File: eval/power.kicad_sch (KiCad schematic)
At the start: 20 parts, among them Q1 BSC0702LS, Q2 BSC0702LS, U2 LM5148RGYR

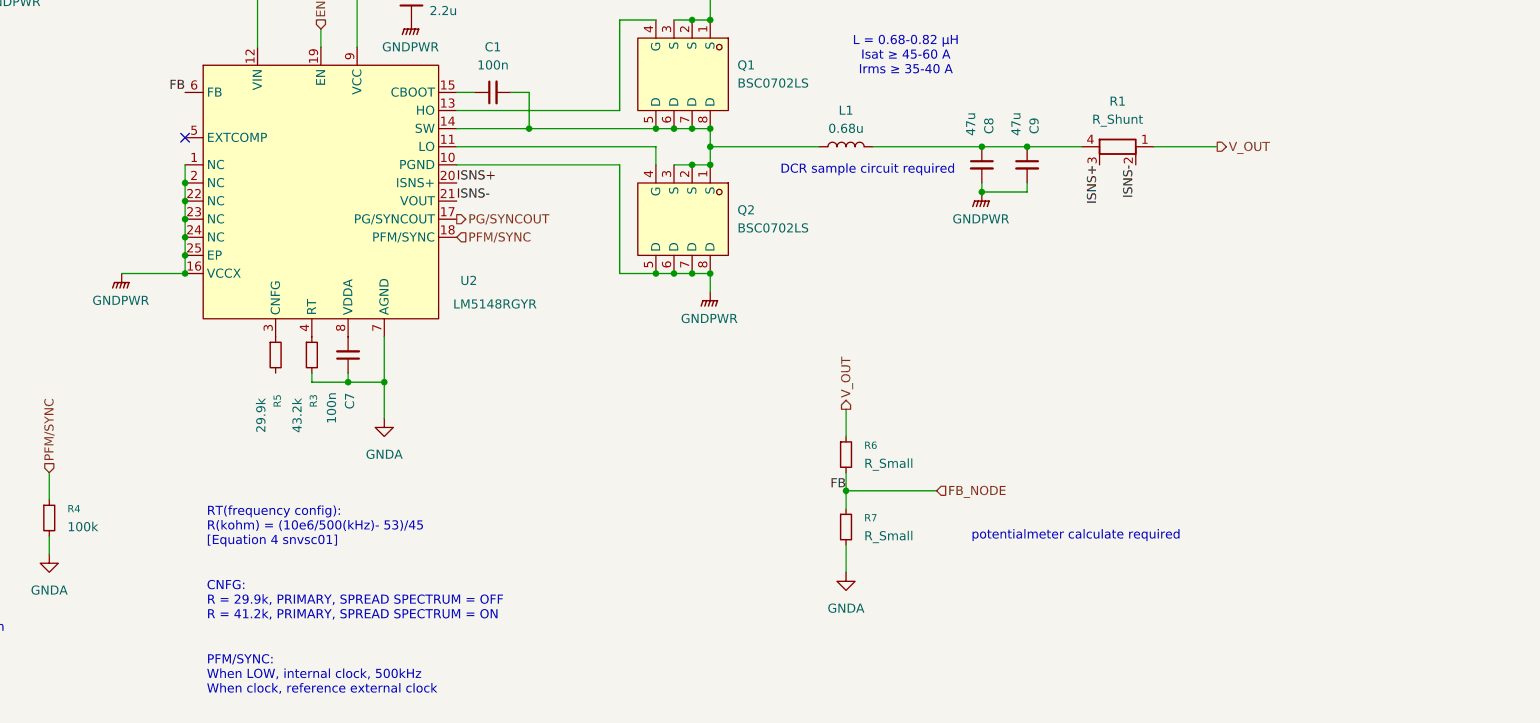
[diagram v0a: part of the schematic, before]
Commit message: Update constant current loop in kicad, base on simluation
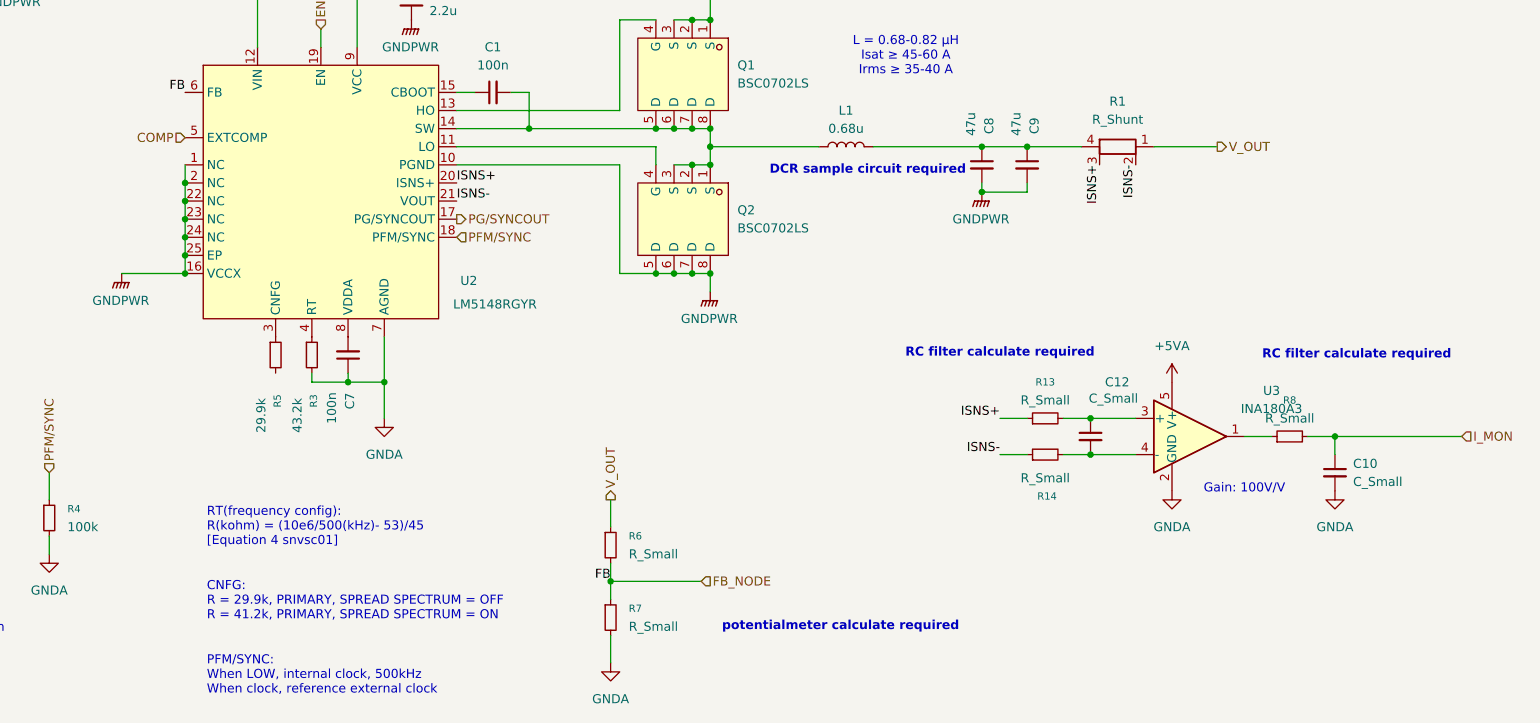
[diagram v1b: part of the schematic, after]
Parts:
- added C10, C12: C_Small, symbol Device:C_Small
- added R13, R14, R8: R_Small, symbol Device:R_Small
- added U3: INA180A3, Package_TO_SOT_SMD:SOT-23-5, symbol Amplifier_Current:INA180A3
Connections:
- net GNDA: now also C10.2, U3.2 (GND)
- net ISNS+: now also R13.1
- net ISNS-: now also R14.1
- net COMP: now reaches U2.5 (EXTCOMP)
- new net: C12.2, R14.2, U3.4 (-)
- new net: C12.1, R13.2, U3.3 (+)
- new net: R8.1, U3.1
- new net +5VA: U3.5 (V+)
- new net I_MON: C10.1, R8.2
- no-connect marks 1 -> 0
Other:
- note added: "Gain: 100V/V"
- note added: "RC filter calculate required"
- moved on the sheet: R6, R7

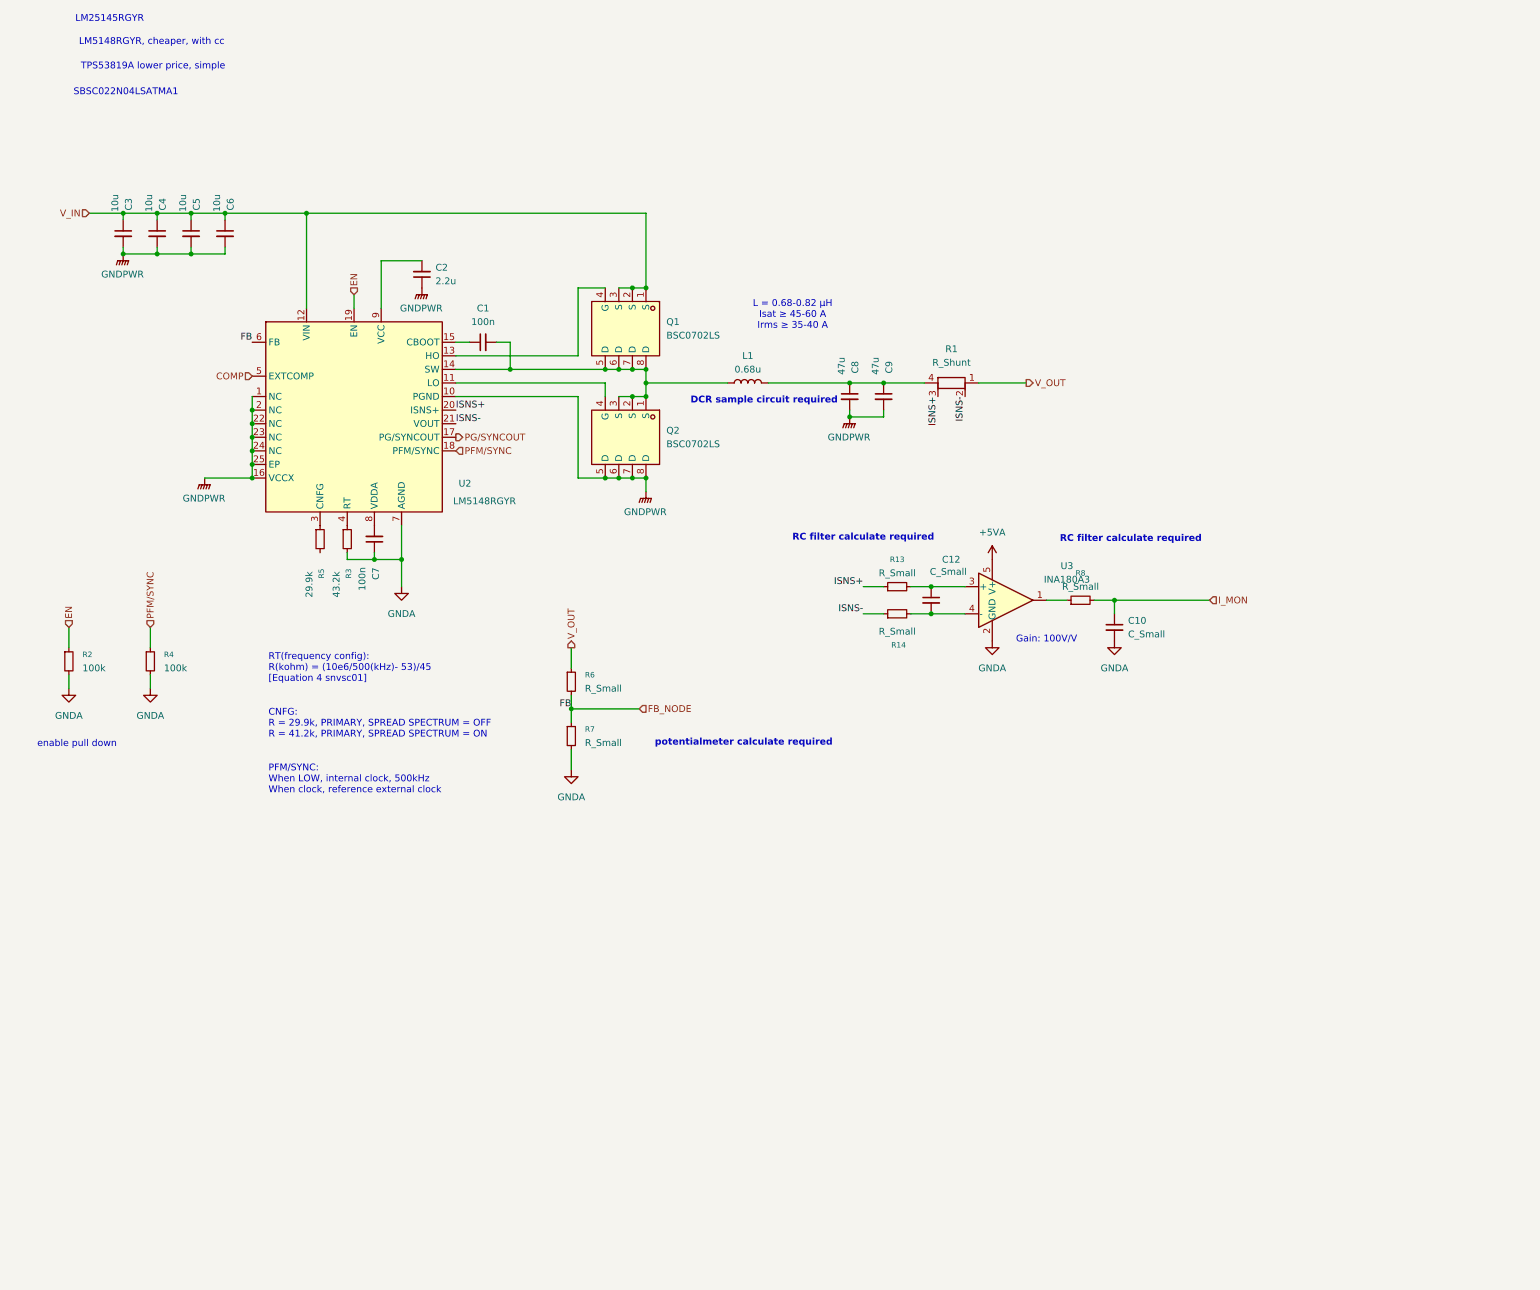
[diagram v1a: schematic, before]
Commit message: Change from G071 to G0B1, add screen, usb
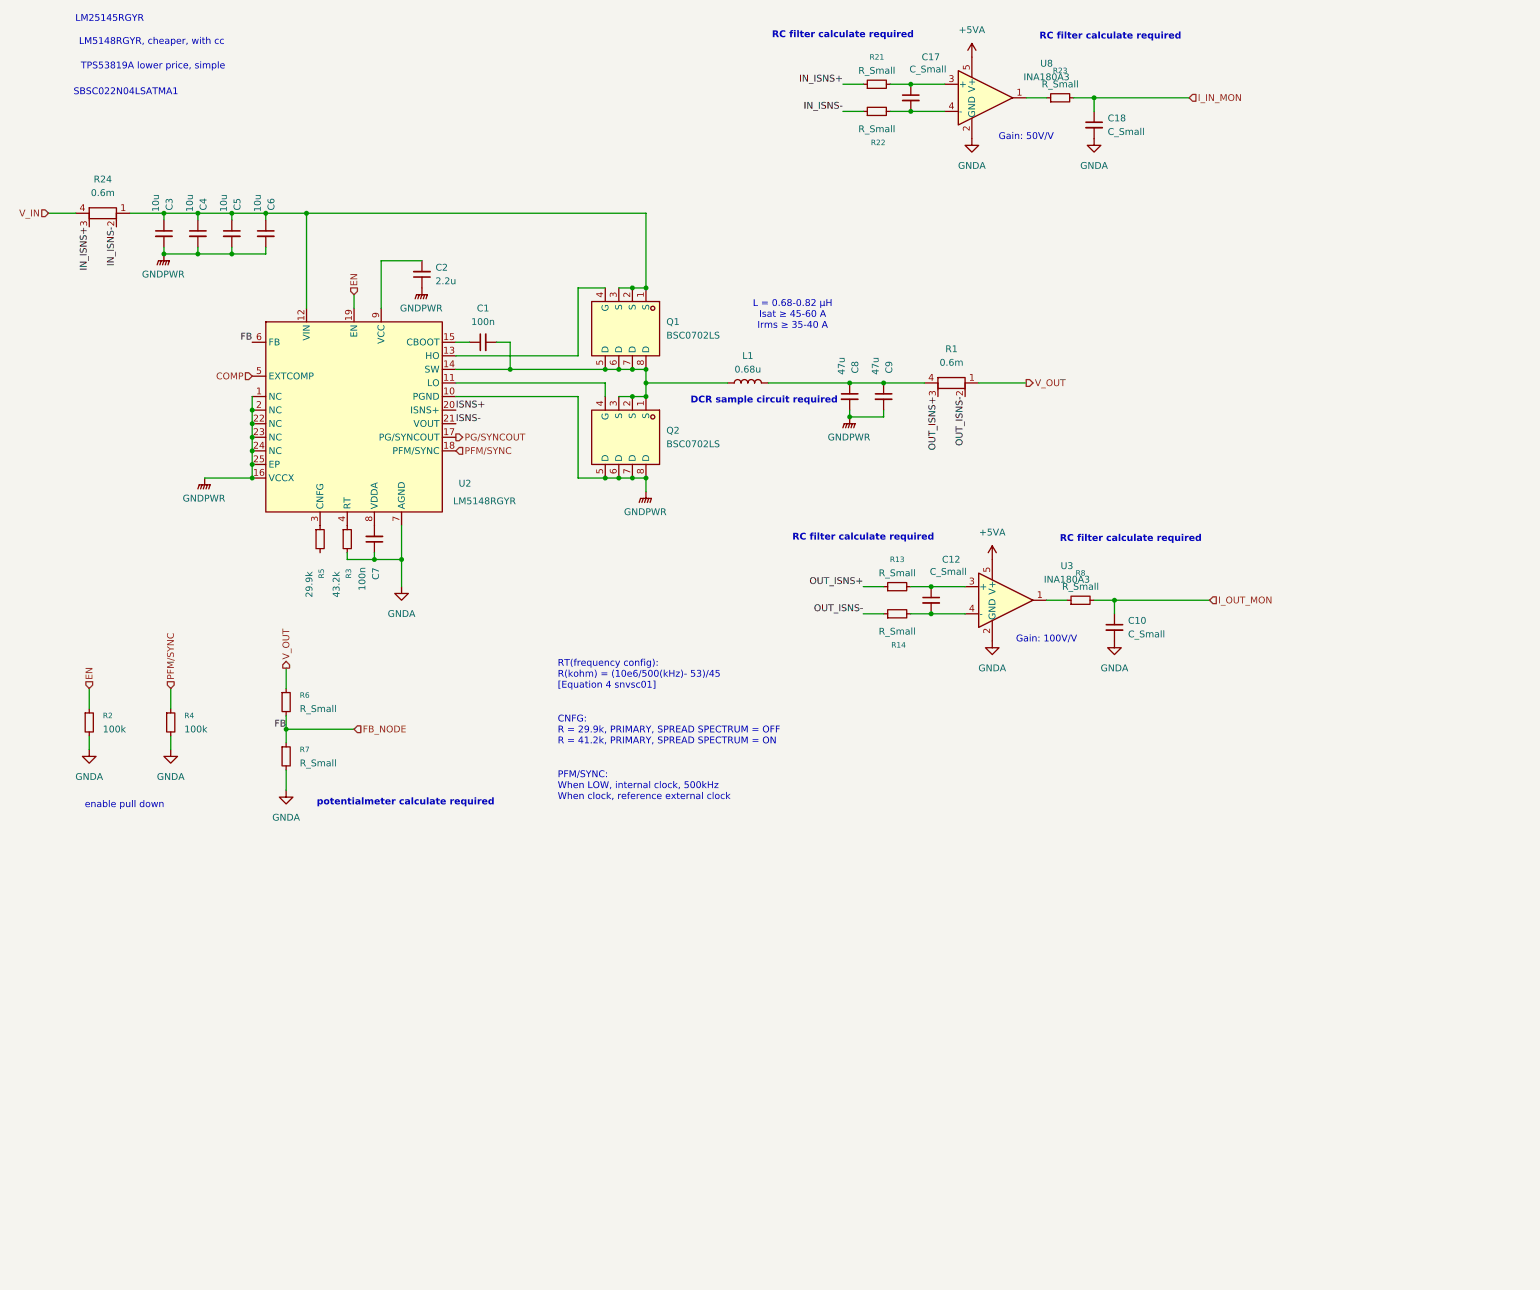
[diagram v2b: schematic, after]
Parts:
- added C17, C18: C_Small, symbol Device:C_Small
- added R21, R22, R23: R_Small, symbol Device:R_Small
- added R24: 0.6m, symbol Device:R_Shunt
- added U8: INA180A3, Package_TO_SOT_SMD:SOT-23-5, symbol Amplifier_Current:INA180A3
- R1: value R_Shunt -> 0.6m
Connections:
- net +5VA: now also U8.5 (V+)
- net GNDA: now also C18.2, U8.2 (GND)
- net ISNS+: no longer R1.3, R13.1
- net ISNS-: no longer R1.2, R14.1
- net V_IN: now also R24.4; no longer C3.1, C4.1, C5.1, C6.1, Q1.1 (S), Q1.2 (S), Q1.3 (S), U2.12 (VIN)
- net I_MON renamed I_OUT_MON
- new net: C17.1, R21.2, U8.3 (+)
- new net: C3.1, C4.1, C5.1, C6.1, Q1.1 (S), Q1.2 (S), Q1.3 (S), R24.1, U2.12 (VIN)
- new net: R23.1, U8.1
- new net: C17.2, R22.2, U8.4 (-)
- new net IN_ISNS+: R21.1, R24.3
- new net IN_ISNS-: R22.1, R24.2
- new net I_IN_MON: C18.1, R23.2
- new net OUT_ISNS+: R1.3, R13.1
- new net OUT_ISNS-: R1.2, R14.1
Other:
- note added: "Gain: 50V/V"
- moved on the sheet: C3, C4, C5, C6, R2, R4, R6, R7

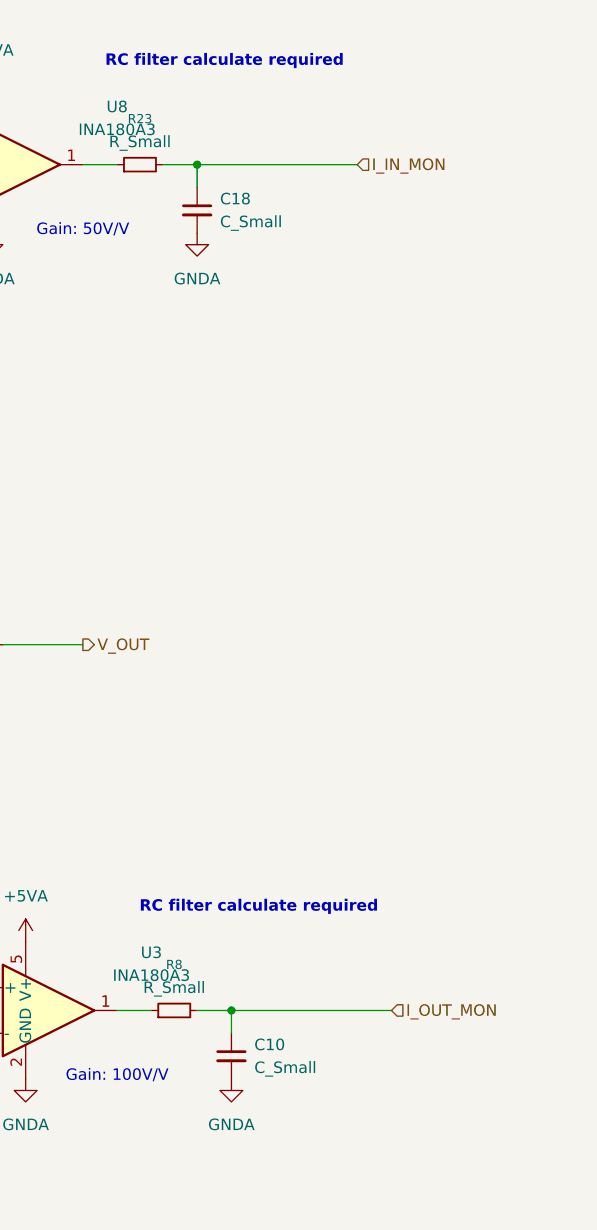
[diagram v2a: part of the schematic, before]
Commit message: Complete most MCU pinout setup
next step power rail and pd
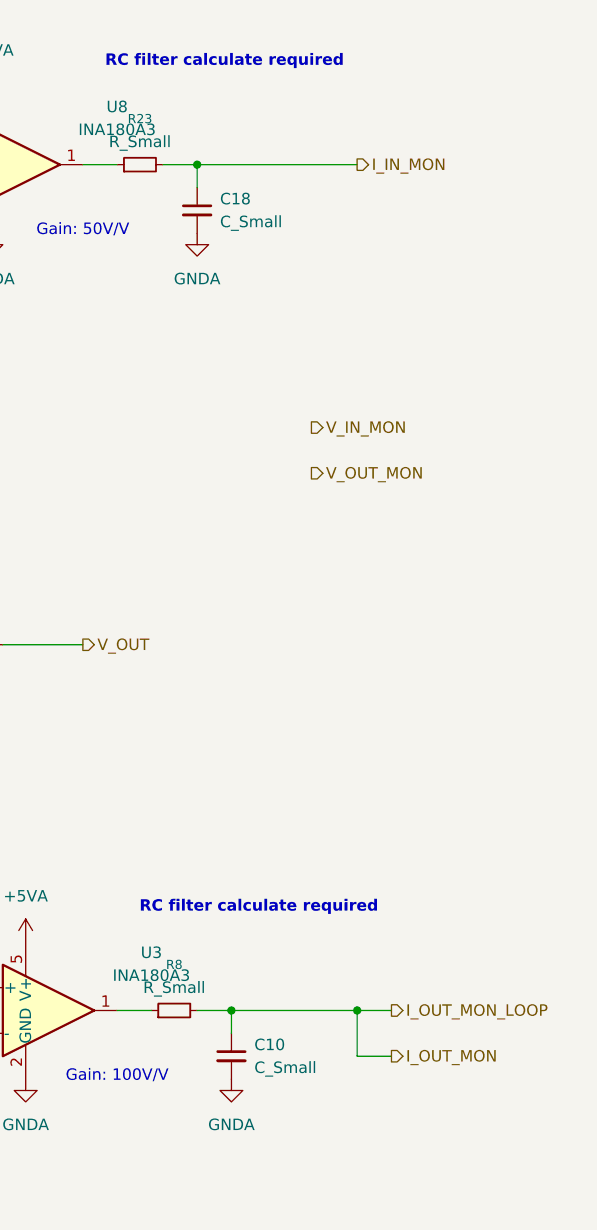
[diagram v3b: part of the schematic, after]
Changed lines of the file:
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@@
 	)
 	(junction
+		(at 234.95 134.62)
+		(diameter 0)
+		(color 0 0 0 0)
+	)
+	(junction
 		(at 59.69 101.6)
 		(diameter 0)
@@
 	(wire
 		(pts
+			(xy 234.95 139.7) (xy 234.95 134.62)
+		)
+		(stroke
+			(width 0)
+			(type default)
+		)
+	)
+	(wire
+		(pts
 			(xy 125.73 93.98) (xy 125.73 96.52)
 		)
@@
 	(wire
 		(pts
+			(xy 234.95 134.62) (xy 238.76 134.62)
+		)
+		(stroke
+			(width 0)
+			(type default)
+		)
+	)
+	(wire
+		(pts
 			(xy 179.07 43.18) (xy 182.88 43.18)
 		)
@@
 	(wire
 		(pts
+			(xy 238.76 139.7) (xy 234.95 139.7)
+		)
+		(stroke
+			(width 0)
+			(type default)
+		)
+	)
+	(wire
+		(pts
 			(xy 49.53 62.23) (xy 43.18 62.23)
 		)
@@
 	(wire
 		(pts
-			(xy 220.98 134.62) (xy 238.76 134.62)
+			(xy 220.98 134.62) (xy 234.95 134.62)
 		)
 		(stroke
@@
 		)
 	)
+	(hierarchical_label "I_OUT_MON"
+		(shape output)
+		(at 238.76 139.7 0)
+		(effects
+			(font
+				(size 1.27 1.27)
+			)
+			(justify left)
+		)
+	)
 	(hierarchical_label "EN"
 		(shape input)
@@
 		)
 	)
+	(hierarchical_label "V_IN_MON"
+		(shape output)
+		(at 229.87 69.85 0)
+		(effects
+			(font
+				(size 1.27 1.27)
+			)
+			(justify left)
+		)
+	)
 	(hierarchical_label "EN"
 		(shape input)
@@
 	)
 	(hierarchical_label "I_IN_MON"
-		(shape input)
+		(shape output)
 		(at 234.95 40.64 0)
 		(effects
@@
 		)
 	)
-	(hierarchical_label "I_OUT_MON"
-		(shape input)
+	(hierarchical_label "I_OUT_MON_LOOP"
+		(shape output)
 		(at 238.76 134.62 0)
 		(effects
 			(font
+				(size 1.27 1.27)
+			)
+			(justify left)
+		)
+	)
+	(hierarchical_label "V_OUT_MON"
+		(shape output)
+		(at 229.87 74.93 0)
+		(effects
+			(font
